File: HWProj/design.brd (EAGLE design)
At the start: 149.8 x 103.8 mm, 69 parts, among them IC1 LM311N, IC10 TL071P, IC11 TL071P, IC12 TL071P, IC13 TL071P, IC14 TL071P, IC15 TL071P, IC16 LM311N, IC17 TL071P, IC18 TL071P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

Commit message: revised board rev0.2
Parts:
- moved TM7 1.27 mm to (63.5, 87.6)
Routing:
- net V+: track 11.2 -> 483.7 mm, vias 0 -> 3
- net N$20: track 46.0 -> 50.3 mm
- net BANDPASS_OUT: track 66.5 -> 65.0 mm
- net GND: track 444.2 -> 445.7 mm
- net N$22: track 37.9 -> 36.6 mm
- net DGNDLVL: track 178.4 -> 179.5 mm
- net N$25: track 62.6 -> 61.8 mm
- removed copper zone on layer 1, net V+
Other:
- board text added: "filter control"
- board text added: "mixer"

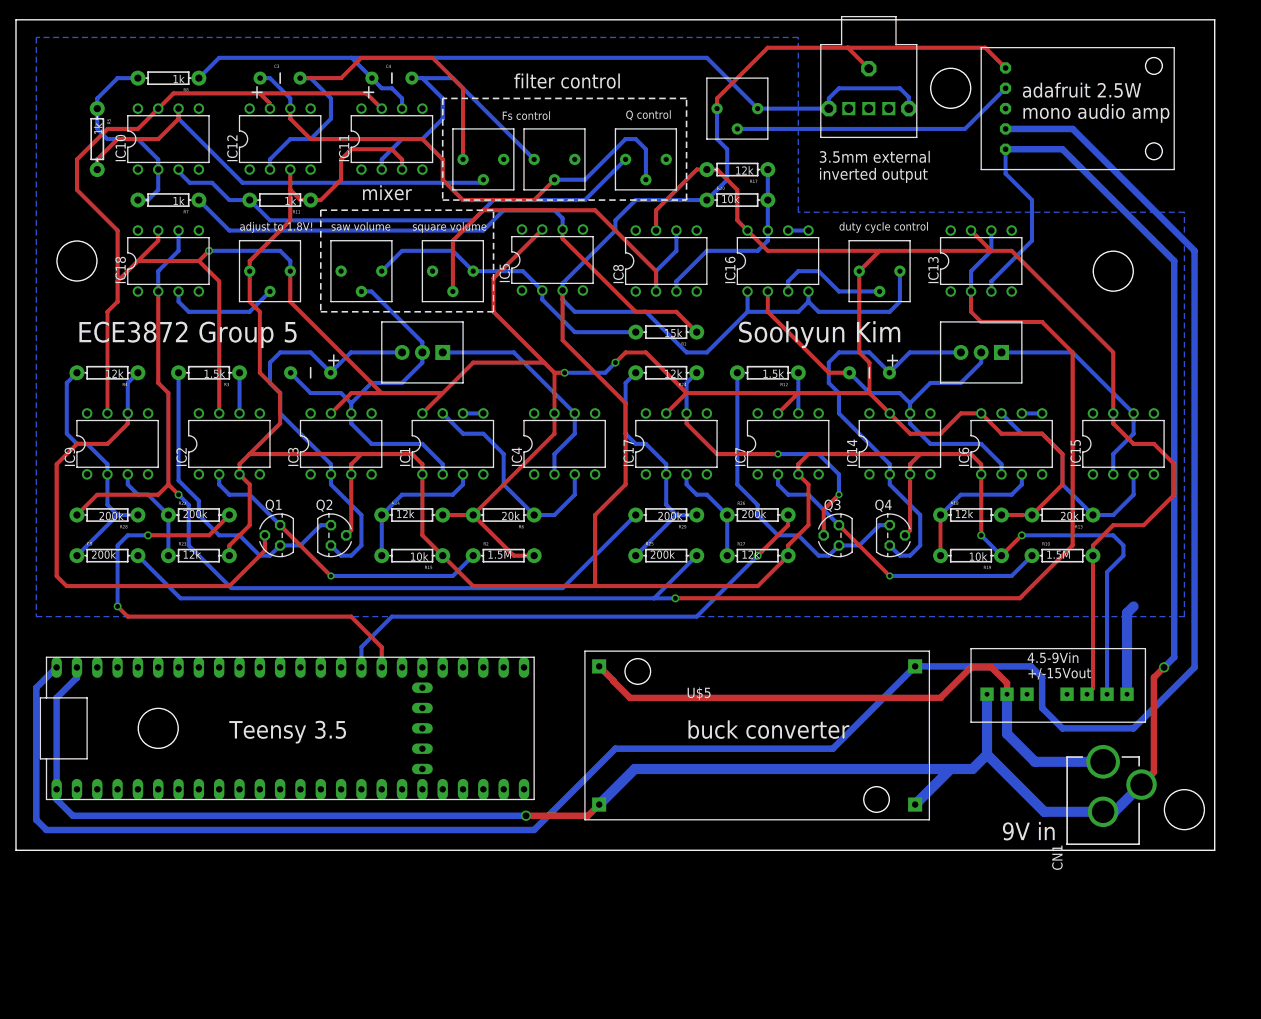
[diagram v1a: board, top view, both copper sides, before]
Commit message: added motor, sensors, and servos--board rev1
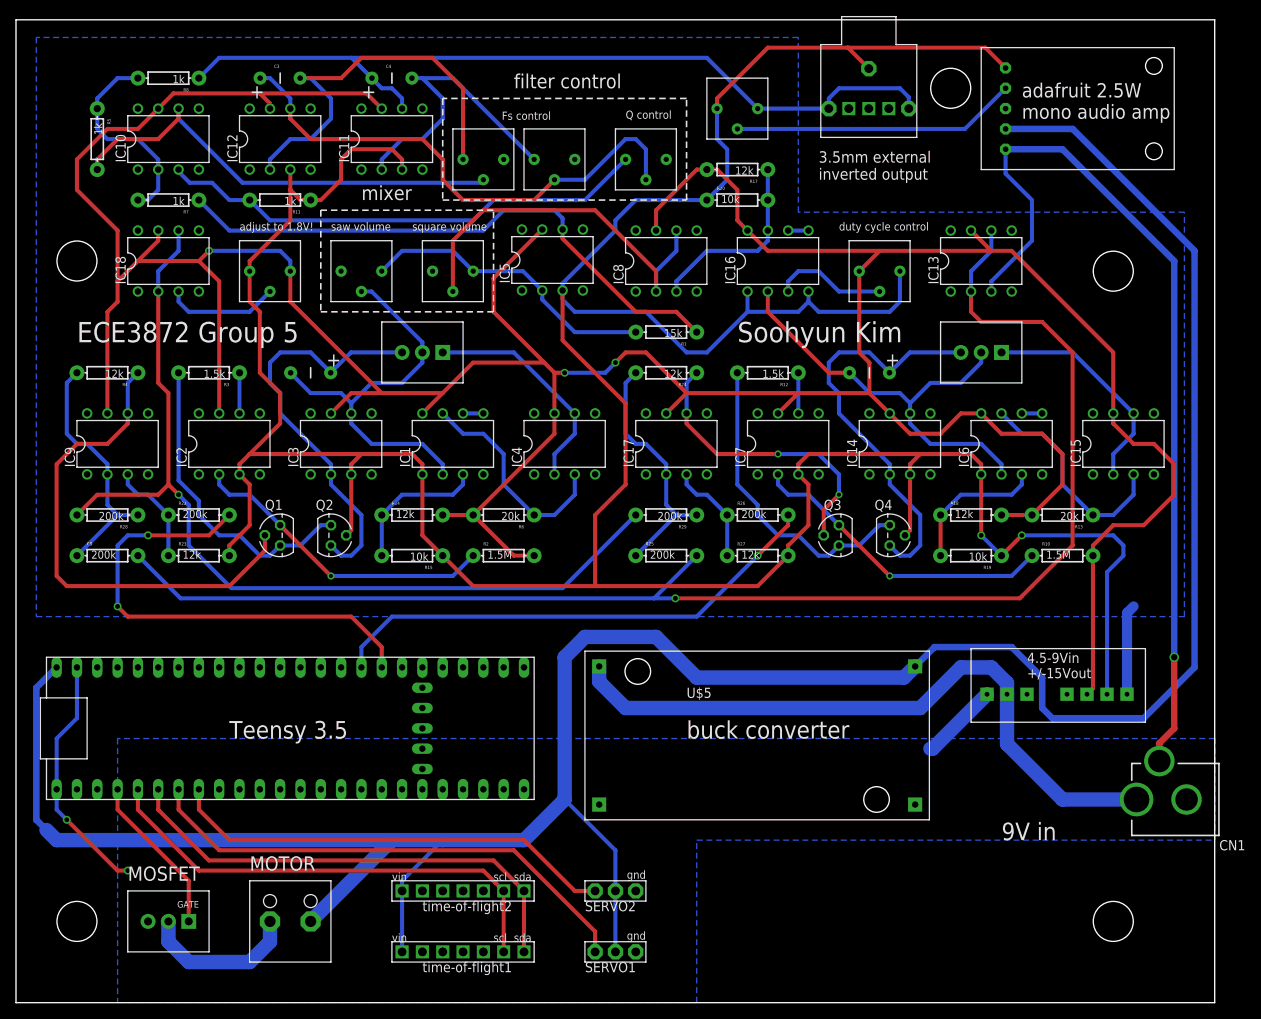
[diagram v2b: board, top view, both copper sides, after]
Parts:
- added U$10: 3872_MOTOR, HyTechDevices:3872_MOTOR
- added U$11: FQP30N06L, HyTechDevices:TO-220
- added U$12, U$13: VL53L0X, HyTechDevices:VL53L0X
- added U$8, U$9: SERVO_3PIN_HEADER, HyTechDevices:SERVO_3PIN_HEADER
- moved CN1 19.9 mm to (153.7, 6.35), turned to 90 degrees
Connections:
- new net MOTOR_PWM: U$11.1, U$4.D2
- new net N$33: U$10.-, U$11.2
- new net SCL: U$12.SCL, U$13.SCL, U$4.D3(CANTX)
- new net SDA: U$12.SDA, U$13.SDA, U$4.D4(CANRX)
- new net SERVO1_PWM: U$4.D5, U$8.CONTROL
- new net SERVO2_PWM: U$4.D6, U$9.CONTROL
- net +5V: now also U$10.+, U$12.VIN, U$13.VIN, U$8.POWER, U$9.POWER
- net DGND: now also U$11.3, U$12.GND, U$13.GND, U$8.GND, U$9.GND
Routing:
- net DGND: track 290.6 -> 152.2 mm, vias 2 -> 3
- net +5V: track 264.5 -> 333.2 mm
- net SERVO1_PWM: track 0.00 -> 63.5 mm
- net SDA: track 0.00 -> 60.1 mm
- net SCL: track 0.00 -> 60.1 mm
- net SERVO2_PWM: track 0.00 -> 56.3 mm
- net MOTOR_PWM: track 0.00 -> 20.2 mm
- net N$33: track 0.00 -> 19.9 mm
- net VCC: track 74.9 -> 83.9 mm
- added copper zone on layer 16, net DGND
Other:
- board size 149.8 x 103.8 mm -> 149.8 x 122.9 mm
- board text added: "GATE"
- board text added: "MOSFET"
- board text added: "MOTOR"
- board text added: "SERVO1"
- board text added: "SERVO2"
- board text added: "time-of-flight1"
- board text added: "time-of-flight2"

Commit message: silkscreen cleanup, tested square generation
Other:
- board text added: "100k"
- board text added: "10k"
- board text added: "50k"
- board text added: "master volume"
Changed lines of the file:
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@@
 <hole x="7.62" y="-8.89" drill="5"/>
 <hole x="137.16" y="-8.89" drill="5"/>
-<text x="123.19" y="1.27" size="2.1844" layer="21">9V in</text>
+<text x="140.97" y="-1.27" size="2.1844" layer="21">9V in</text>
 <text x="83.82" y="13.97" size="2.1844" layer="21">buck converter</text>
 <text x="7.62" y="63.5" size="2.54" layer="21">ECE3872 Group 5</text>
@@
 <text x="50.8" y="-7.62" size="1.27" layer="21">time-of-flight2</text>
 <text x="50.8" y="-15.24" size="1.27" layer="21">time-of-flight1</text>
+<text x="57.15" y="87.63" size="1.4224" layer="21">50k</text>
+<text x="66.04" y="87.63" size="1.4224" layer="21">50k</text>
+<text x="77.47" y="87.63" size="1.4224" layer="21">50k</text>
+<text x="86.36" y="97.79" size="1.016" layer="21">master volume</text>
+<text x="88.9" y="93.98" size="1.4224" layer="21">50k</text>
+<text x="53.34" y="73.66" size="1.4224" layer="21">50k</text>
+<text x="41.91" y="73.66" size="1.4224" layer="21">50k</text>
+<text x="30.48" y="73.66" size="1.4224" layer="21">100k</text>
+<text x="106.68" y="73.66" size="1.4224" layer="21">10k</text>
+<text x="124.46" y="64.77" size="0.8128" layer="21" rot="R180">GATE</text>
+<text x="54.61" y="64.77" size="0.8128" layer="21" rot="R180">GATE</text>
 </plain>
 <attributes>

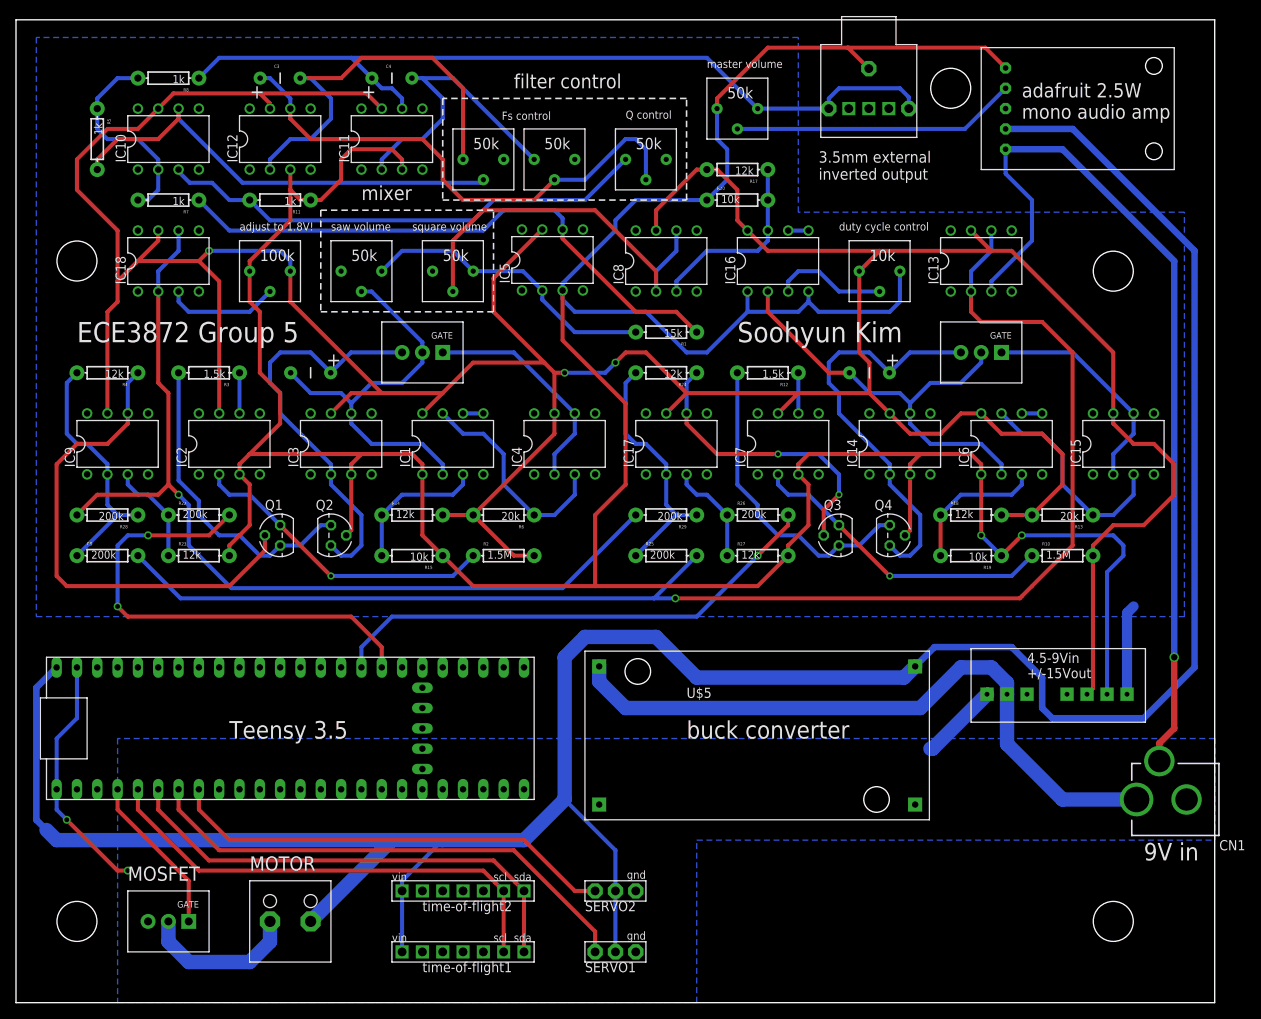
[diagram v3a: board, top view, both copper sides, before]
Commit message: added fuses, shunt system, finalized board rev1.1
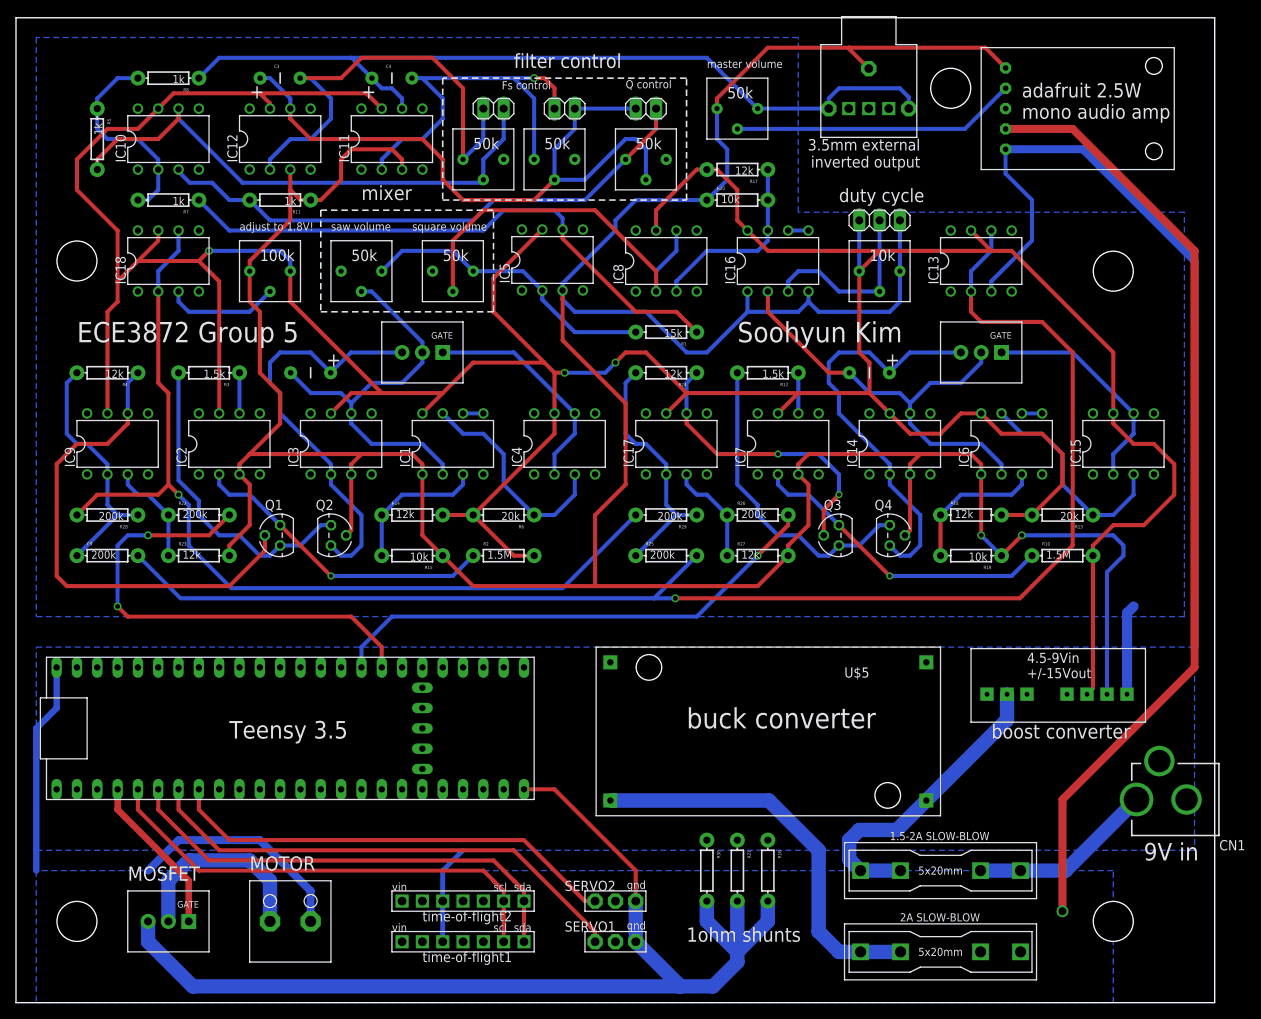
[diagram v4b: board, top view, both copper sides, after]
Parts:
- added POT1_EXT, POT2_EXT, POT3_EXT: M02, HyTechDevices:1X02
- added POT4_EXT: (no value), HyTechDevices:1X03
- added R16, R21, R30: (no value), HyTechDevices:AXIAL-0.3
- added U$14, U$15: (no value), HyTechDevices:0751.0110
- moved U$5 49.4 mm to (115.6, 25.4), turned to 180 degrees
- moved U$12 1.27 mm to (47.0, -12.7)
- moved U$13 1.27 mm to (47.0, -7.62)
- moved U$8 1.27 mm to (72.4, -11.4)
- moved U$9 1.27 mm to (72.4, -6.35)
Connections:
- new net N$29: U$14.R1, U$14.R2, U$5.+IN, U$7.2
- new net N$32: U$15.L1, U$15.L2, U$5.+OUT
- new net SHUNT_ADC_POLL: R16.P$2, R21.P$2, R30.P$2, U$11.3, U$4.A13, U$8.GND, U$9.GND
- net +5V: now also U$15.R1, U$15.R2; no longer U$5.+OUT
- net BANDPASS_OUT: now also POT2_EXT.1, POT3_EXT.1
- net DGND: now also R16.P$1, R21.P$1, R30.P$1; no longer U$11.3, U$8.GND, U$9.GND
- net GND: now also POT4_EXT.1
- net HIGHPASS_OUT: now also POT1_EXT.1
- net N$20: now also POT1_EXT.2
- net N$22: now also POT2_EXT.2
- net N$25: now also POT3_EXT.2
- net N$26: now also POT4_EXT.2
- net V+: now also POT4_EXT.3
- net VCC: now also U$14.L1, U$14.L2; no longer U$5.+IN, U$7.2
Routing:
- net +5V: track 333.2 -> 174.1 mm, vias 0 -> 1
- net SHUNT_ADC_POLL: track 0.00 -> 138.2 mm
- net VCC: track 83.9 -> 23.2 mm
- net N$32: track 0.00 -> 50.1 mm
- net DGND: track 152.2 -> 111.4 mm, vias 3 -> 0
- net N$29: track 0.00 -> 38.6 mm
- net BANDPASS_OUT: track 65.0 -> 82.6 mm
- net N$22: track 36.6 -> 49.2 mm, vias 0 -> 1
- net HIGHPASS_OUT: track 57.6 -> 67.6 mm
- net N$26: track 14.3 -> 23.2 mm
- net N$25: track 61.8 -> 69.7 mm
- net N$20: track 50.3 -> 57.7 mm
- net V+: track 483.7 -> 490.0 mm
- net GND: track 445.7 -> 451.7 mm
- net N$33: track 19.9 -> 25.0 mm
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- added copper zone on layer 16, net +5V
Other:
- board size 149.8 x 122.9 mm -> 149.8 x 123.1 mm
- board text added: "1.5-2A SLOW-BLOW"
- board text added: "1ohm shunts"
- board text added: "2A SLOW-BLOW"
- board text added: "boost converter"
- board text added: "duty cycle"
- board text removed: "duty cycle control"

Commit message: attempted integration of buttons and servos
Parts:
- added LED, PAUSE, PLAY, POWER, REC: M02, HyTechDevices:1X02
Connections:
- net +1.8V renamed +1.7V
- new net LED: LED.2, U$4.D0(RX1)
- new net PAUSE: PAUSE.2, U$4.A16
- new net PLAY: PLAY.2, U$4.A15
- new net POWER: POWER.2, U$4.A14
- new net RECORD: REC.2, U$4.A17
- net DGND: now also LED.1, PAUSE.1, PLAY.1, POWER.1, REC.1
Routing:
- net RECORD: track 0.00 -> 18.2 mm
- net PAUSE: track 0.00 -> 13.5 mm
- net PLAY: track 0.00 -> 8.15 mm
- net LED: track 0.00 -> 5.61 mm
- net POWER: track 0.00 -> 4.86 mm
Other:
- board text added: "adjust to 1.7V!"
- board text added: "button connections ->"
- board text removed: "adjust to 1.8V!"
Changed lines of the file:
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@@
 <?xml version="1.0" encoding="utf-8"?>
 <!DOCTYPE eagle SYSTEM "eagle.dtd">
-<eagle version="9.5.2">
+<eagle version="9.6.0">
 <drawing>
 <settings>
@@
 <text x="49.53" y="77.47" size="1.016" layer="21">square volume</text>
 <text x="39.37" y="77.47" size="1.016" layer="21">saw volume</text>
-<text x="27.94" y="77.47" size="1.016" layer="21">adjust to 1.8V!</text>
+<text x="27.94" y="77.47" size="1.016" layer="21">adjust to 1.7V!</text>
 <text x="76.2" y="95.25" size="1.016" layer="21">Q control</text>
 <text x="60.325" y="95.123" size="1.016" layer="21"> Fs control</text>
@@
 <text x="110.49" y="-8.89" size="1.016" layer="21">2A SLOW-BLOW</text>
 <text x="109.22" y="1.27" size="1.016" layer="21">1.5-2A SLOW-BLOW</text>
+<text x="48.26" y="25.4" size="1.27" layer="21">button connections -&gt;</text>
+<wire x1="71.882" y1="27.559" x2="65.405" y2="27.559" width="0.127" layer="21" style="shortdash"/>
+<wire x1="65.405" y1="27.559" x2="65.405" y2="6.35" width="0.127" layer="21" style="shortdash"/>
+<wire x1="65.405" y1="6.35" x2="71.882" y2="6.35" width="0.127" layer="21" style="shortdash"/>
+<wire x1="71.882" y1="6.35" x2="71.882" y2="27.559" width="0.127" layer="21" style="shortdash"/>
 </plain>
 <attributes>
@@
 <element name="U$14" library="HyTechDevices" package="0751.0110" value="" x="115.57" y="-2.54" smashed="yes" rot="R180"/>
 <element name="U$15" library="HyTechDevices" package="0751.0110" value="" x="115.57" y="-12.7" smashed="yes"/>
+<element name="POWER" library="HyTechDevices" package="1X02" value="M02" x="68.58" y="25.4" smashed="yes" rot="R180">
+<attribute name="NAME" x="71.1962" y="23.5712" size="1.016" layer="25" ratio="10" rot="R180"/>
+</element>
+<element name="PLAY" library="HyTechDevices" package="1X02" value="M02" x="68.58" y="20.32" smashed="yes" rot="R180">
+<attribute name="NAME" x="71.1962" y="18.4912" size="1.016" layer="25" ratio="10" rot="R180"/>
+</element>
+<element name="PAUSE" library="HyTechDevices" package="1X02" value="M02" x="68.58" y="15.24" smashed="yes" rot="R180">
+<attribute name="NAME" x="71.1962" y="13.4112" size="1.016" layer="25" ratio="10" rot="R180"/>
+</element>
+<element name="REC" library="HyTechDevices" package="1X02" value="M02" x="68.58" y="10.16" smashed="yes" rot="R180">
+<attribute name="NAME" x="71.1962" y="8.3312" size="1.016" layer="25" ratio="10" rot="R180"/>
+</element>
+<element name="LED" library="HyTechDevices" package="1X02" value="M02" x="7.62" y="2.54" smashed="yes">
+<attribute name="NAME" x="6.2738" y="4.3688" size="1.016" layer="25" ratio="10"/>
+</element>
 </elements>
 <signals>
@@
 <wire x1="123.7" y1="87.63" x2="133.35" y2="87.63" width="1" layer="16"/>
 <wire x1="147.32" y1="73.66" x2="147.32" y2="25.4" width="1" layer="16"/>
+<contactref element="POWER" pad="1"/>
+<contactref element="PLAY" pad="1"/>
+<contactref element="PAUSE" pad="1"/>
+<contactref element="REC" pad="1"/>
+<contactref element="LED" pad="1"/>
 </signal>
 <signal name="VCC">
@@
 <wire x1="100.965" y1="42.545" x2="100.965" y2="39.37" width="0.508" layer="1"/>
 </signal>
-<signal name="+1.8V">
+<signal name="+1.7V">
 <contactref element="R29" pad="P$2"/>
 <contactref element="R28" pad="P$2"/>
@@
 <wire x1="105.57" y1="-12.7" x2="110.57" y2="-12.7" width="1.8" layer="16"/>
 </signal>
+<signal name="POWER">
+<contactref element="U$4" pad="A14"/>
+<contactref element="POWER" pad="2"/>
+<wire x1="63.5" y1="22.86" x2="66.04" y2="25.4" width="0.4064" layer="16"/>
+<wire x1="66.04" y1="25.4" x2="67.31" y2="25.4" width="0.4064" layer="16"/>
+</signal>
+<signal name="PLAY">
+<contactref element="U$4" pad="A15"/>
+<contactref element="PLAY" pad="2"/>
+<wire x1="67.31" y1="20.32" x2="62.23" y2="20.32" width="0.4064" layer="16"/>
+<wire x1="62.23" y1="20.32" x2="60.96" y2="21.59" width="0.4064" layer="16"/>
+<wire x1="60.96" y1="21.59" x2="60.96" y2="22.86" width="0.4064" layer="16"/>
+</signal>
+<signal name="PAUSE">
+<contactref element="U$4" pad="A16"/>
+<contactref element="PAUSE" pad="2"/>
+<wire x1="67.31" y1="15.24" x2="63.5" y2="15.24" width="0.4064" layer="16"/>
+<wire x1="63.5" y1="15.24" x2="58.42" y2="20.32" width="0.4064" layer="16"/>
+<wire x1="58.42" y1="20.32" x2="58.42" y2="22.86" width="0.4064" layer="16"/>
+</signal>
+<signal name="RECORD">
+<contactref element="U$4" pad="A17"/>
+<contactref element="REC" pad="2"/>
+<wire x1="67.31" y1="10.16" x2="66.04" y2="10.16" width="0.4064" layer="16"/>
+<wire x1="66.04" y1="10.16" x2="55.88" y2="20.32" width="0.4064" layer="16"/>
+<wire x1="55.88" y1="20.32" x2="55.88" y2="22.86" width="0.4064" layer="16"/>
+</signal>
+<signal name="LED">
+<contactref element="LED" pad="2"/>
+<contactref element="U$4" pad="D0(RX1)"/>
+<wire x1="8.89" y1="2.54" x2="8.89" y2="5.08" width="0.6096" layer="16"/>
+<wire x1="8.89" y1="5.08" x2="7.62" y2="6.35" width="0.6096" layer="16"/>
+<wire x1="7.62" y1="6.35" x2="7.62" y2="7.62" width="0.6096" layer="16"/>
+</signal>
 </signals>
